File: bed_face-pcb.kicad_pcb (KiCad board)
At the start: 2 copper layers, 98 parts, among them SW1 SW_Push, U1 ProMicro

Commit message: keys placed * may change to my personal layout
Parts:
- moved D37 359.0 mm to (53.2, 132.6), turned to 270 degrees
- moved D25 352.9 mm to (53.2, 113.5), turned to 270 degrees
- moved D38 351.2 mm to (72.2, 132.6), turned to 270 degrees
- moved D39 320.8 mm to (91.3, 132.6), turned to 270 degrees
- moved SW1 298.3 mm to (81.0, 57.1)
- moved D16 294.2 mm to (110.3, 94.5), turned to 270 degrees
- moved D17 287.0 mm to (129.4, 94.5), turned to 270 degrees
- moved D27 280.5 mm to (91.3, 113.5), turned to 270 degrees
- moved D18 269.1 mm to (148.4, 94.5), turned to 270 degrees
- moved D40 265.7 mm to (110.3, 132.6), turned to 270 degrees
- moved D5 261.0 mm to (129.4, 75.4), turned to 270 degrees
- moved D26 256.6 mm to (72.2, 113.6), turned to 270 degrees
- moved D30 249.2 mm to (148.4, 113.5), turned to 270 degrees
- moved D32 239.3 mm to (186.5, 113.5), turned to 270 degrees
- moved D31 233.2 mm to (167.5, 113.5), turned to 270 degrees
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- renumbered D37 to D10, D41 to D11, D45 to D12, D2 to D13, D6 to D14, D10 to D15, D14 to D16, D18 to D17, D22 to D18, D26 to D19, D5 to D2, D30 to D20, D34 to D21, D38 to D22, D42 to D23, D46 to D24, D3 to D25, D7 to D26, D11 to D27, D15 to D28, D19 to D29, D9 to D3, D23 to D30, D27 to D31, D31 to D32, D35 to D33, D39 to D34, D43 to D35, D47 to D36, D4 to D37, D8 to D38, D12 to D39, D13 to D4, D16 to D40, D20 to D41, D24 to D42, D28 to D43, D32 to D44, D36 to D45, D40 to D46, D44 to D47, D17 to D5, D21 to D6, D25 to D7, D29 to D8, D33 to D9, MX37 to MX10, MX41 to MX11, MX45 to MX12, MX2 to MX13, MX6 to MX14, MX10 to MX15, MX14 to MX16, MX18 to MX17, MX22 to MX18, MX26 to MX19, MX5 to MX2, MX30 to MX20, MX34 to MX21, MX38 to MX22, MX42 to MX23, MX46 to MX24, MX3 to MX25, MX7 to MX26, MX11 to MX27, MX15 to MX28, MX19 to MX29, MX9 to MX3, MX23 to MX30, MX27 to MX31, MX31 to MX32, MX35 to MX33, MX39 to MX34, MX43 to MX35, MX47 to MX36, MX4 to MX37, MX8 to MX38, MX12 to MX39, MX13 to MX4, MX16 to MX40, MX20 to MX41, MX24 to MX42, MX28 to MX43, MX32 to MX44, MX36 to MX45, MX40 to MX46, MX44 to MX47, MX17 to MX5, MX21 to MX6, MX25 to MX7, MX29 to MX8, MX33 to MX9

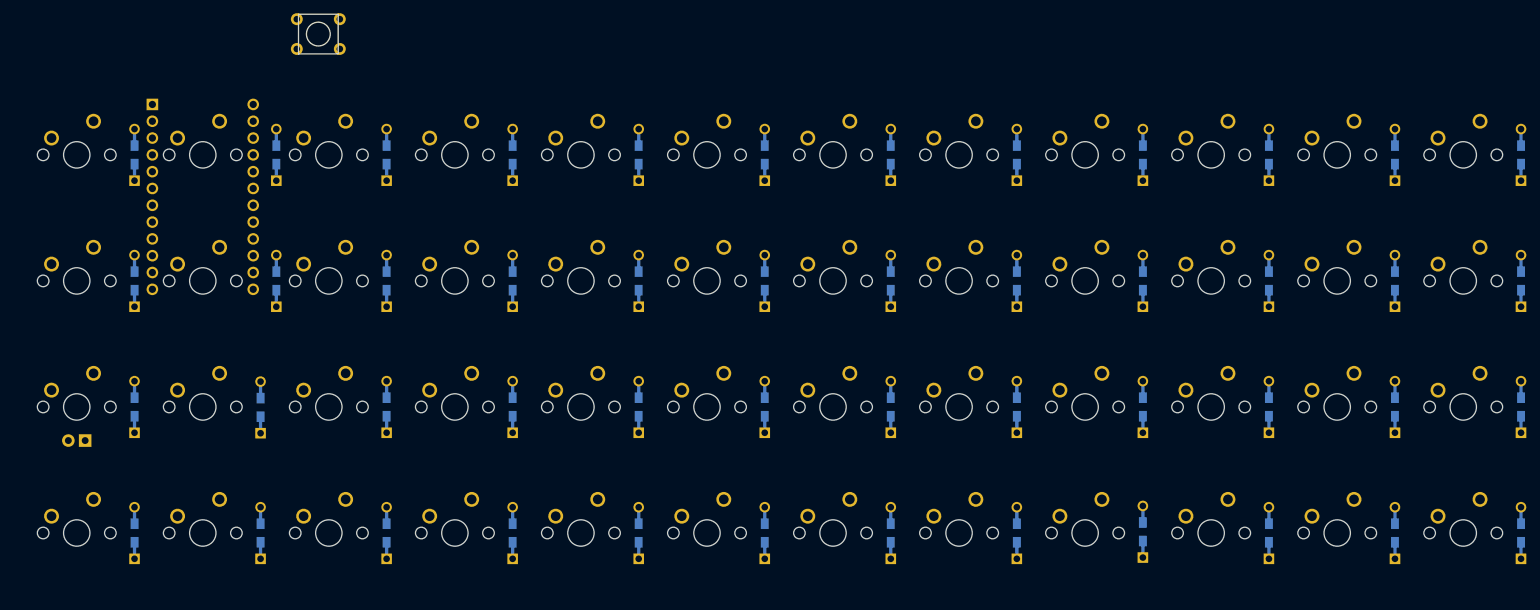
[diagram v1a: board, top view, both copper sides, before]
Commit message: styled switch footprints, initial pcb placement
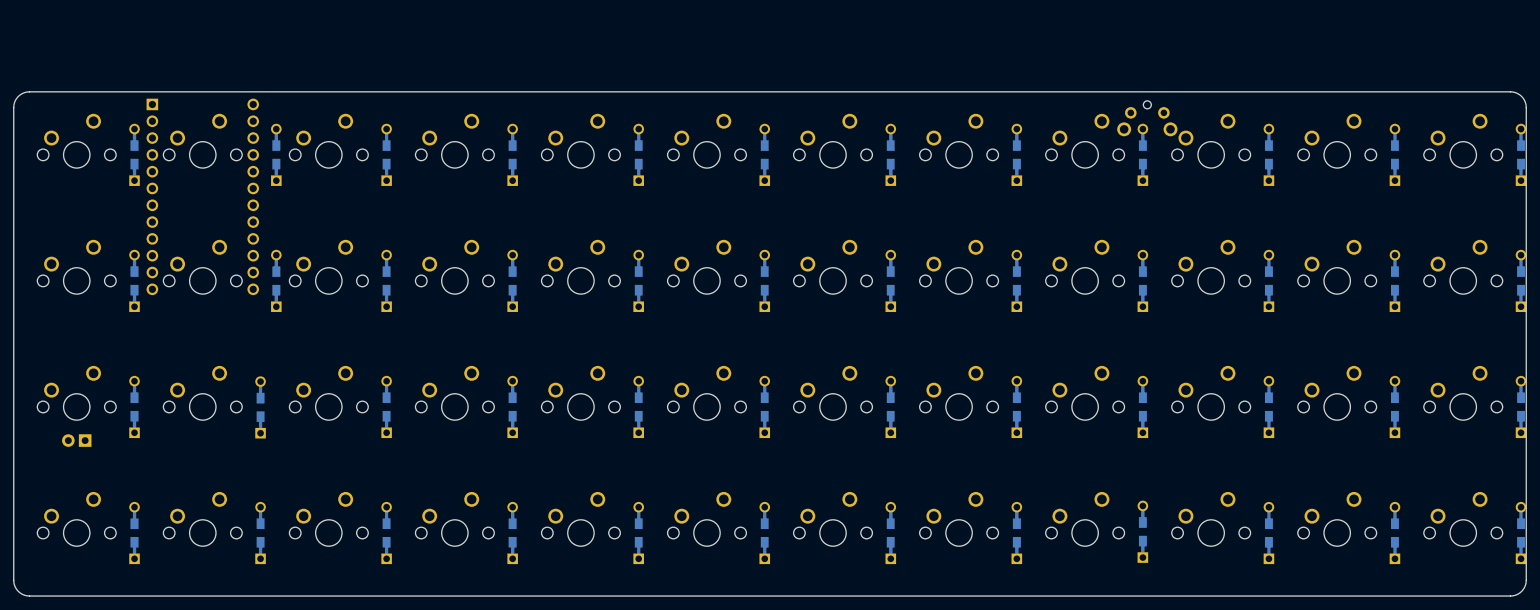
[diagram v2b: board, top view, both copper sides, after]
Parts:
- MX1, MX10, MX11, MX12, MX13, MX14, MX15, MX16, MX17, MX18, MX19, MX2, MX20, MX21, MX22, MX23, MX24, MX26, MX27, MX28, MX29, MX3, MX30, MX31, MX32, MX33, MX34, MX35, MX36, MX37, MX38, MX39, MX4, MX40, MX41, MX42, MX43, MX44, MX45, MX46, MX47, MX48, MX5, MX6, MX7, MX8, MX9: footprint MX_Only:MXOnly-1U-NoLED -> MX_Only:MXOnly-1U-NoLED-EDIT
- MX25: footprint MX_Only:MXOnly-1U -> MX_Only:MXOnly-1U-EDIT
- SW1: footprint random-keyboard-parts:PushButton_6x6mm_TH_Pretty -> Keebio-Parts:SW_Tactile_SPST_Angled_MJTP1117; moved to B.Cu
- moved SW1 128.3 mm to (208.8, 69.1), turned to 180 degrees
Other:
- board outline added: 228.6 x 76.2 mm

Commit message: added +5V, GND to Power net w/ 15 mil track width
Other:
- net class Power added: clearance 0.2, trace_width 0.381, via_dia 0.8, via_drill 0.4
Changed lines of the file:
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@@
     (uvia_dia 0.3)
     (uvia_drill 0.1)
-    (add_net +5V)
     (add_net COL0)
     (add_net COL1)
@@
     (add_net COL8)
     (add_net COL9)
-    (add_net GND)
     (add_net LEDPIN)
     (add_net "Net-(D1-Pad2)")
@@
     (add_net ROW3)
   )
+  (net_class Power ""
+    (clearance 0.2)
+    (trace_width 0.381)
+    (via_dia 0.8)
+    (via_drill 0.4)
+    (uvia_dia 0.3)
+    (uvia_drill 0.1)
+    (add_net +5V)
+    (add_net GND)
+  )
   (module MX_Only:MXOnly-1U-NoLED-EDIT (layer F.Cu)

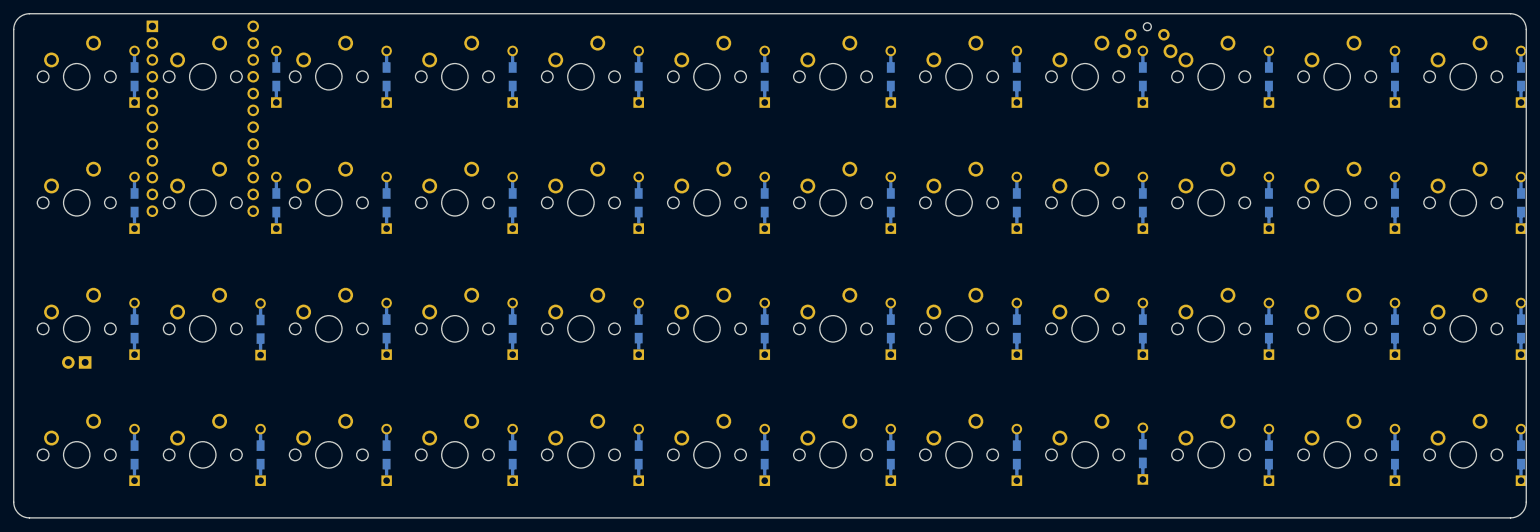
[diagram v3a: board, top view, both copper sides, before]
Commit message: matrix routed, GND fill placed * still needs resistor for LED? * need to add silkscreen/graphic
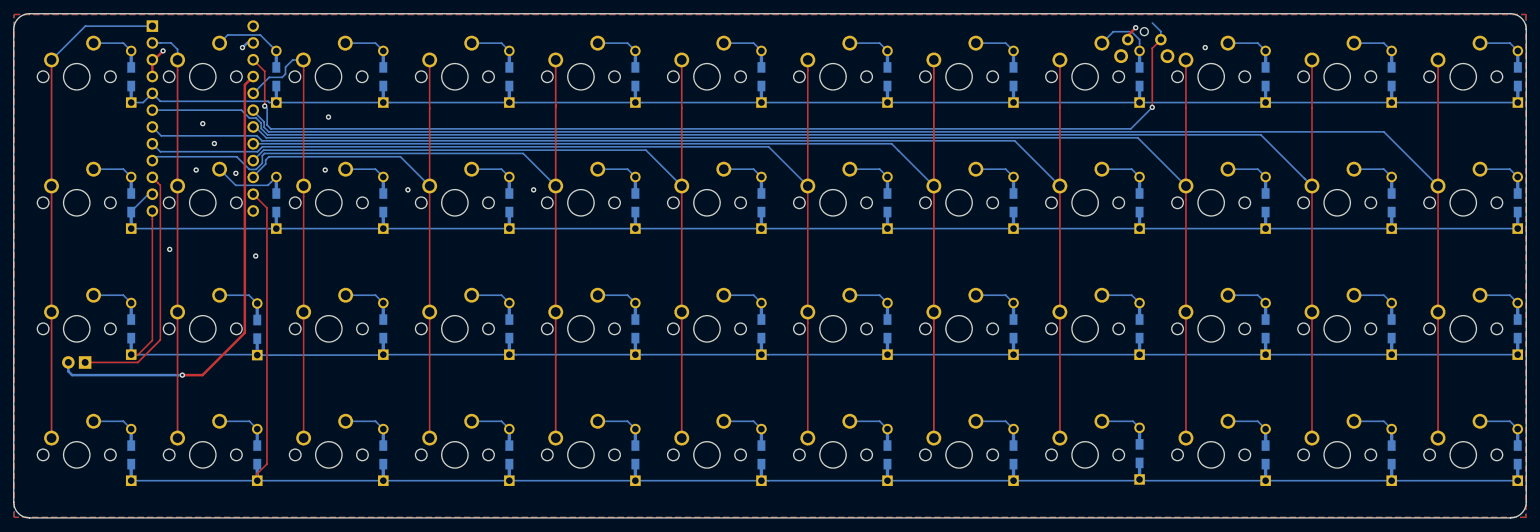
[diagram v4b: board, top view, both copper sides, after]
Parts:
- moved SW1 0.87 mm to (208.3, 69.8)
- moved D1 0.50 mm to (52.7, 75.4)
- moved D10 0.50 mm to (224.1, 75.4)
- moved D11 0.50 mm to (243.2, 75.4)
- moved D13 0.50 mm to (52.7, 94.5)
- moved D15 0.50 mm to (90.8, 94.5)
- moved D16 0.50 mm to (109.8, 94.5)
- moved D17 0.50 mm to (128.9, 94.5)
- moved D18 0.50 mm to (147.9, 94.5)
- moved D19 0.50 mm to (167.0, 94.5)
- moved D20 0.50 mm to (186.0, 94.5)
- moved D21 0.50 mm to (205.1, 94.5)
- moved D22 0.50 mm to (224.1, 94.5)
- moved D23 0.50 mm to (243.2, 94.5)
- moved D24 0.50 mm to (262.2, 94.5)
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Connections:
- net Net-(SW1-Pad1) renamed RESET
- U1 pad 1: Net-(U1-Pad1) -> COL0
- U1 pad 10: Net-(U1-Pad10) -> LEDPIN
- U1 pad 11: Net-(U1-Pad11) -> ROW1
- U1 pad 12: Net-(U1-Pad12) -> ROW2
- U1 pad 14: Net-(U1-Pad14) -> ROW3
- U1 pad 15: Net-(U1-Pad15) -> COL3
- U1 pad 16: Net-(U1-Pad16) -> COL5
- U1 pad 17: Net-(U1-Pad17) -> COL7
- U1 pad 18: Net-(U1-Pad18) -> COL9
- U1 pad 19: Net-(U1-Pad19) -> COL11
- U1 pad 2: Net-(U1-Pad2) -> COL1
- U1 pad 20: Net-(U1-Pad20) -> COL2
- U1 pad 5: Net-(U1-Pad5) -> ROW0
- U1 pad 6: Net-(U1-Pad6) -> COL10
- U1 pad 7: Net-(U1-Pad7) -> COL8
- U1 pad 8: Net-(U1-Pad8) -> COL6
- U1 pad 9: Net-(U1-Pad9) -> COL4
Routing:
- net ROW3: track 0.00 -> 254.5 mm
- net COL11: track 0.00 -> 241.9 mm
- net COL10: track 0.00 -> 238.0 mm
- net ROW2: track 0.00 -> 233.3 mm
- net ROW1: track 0.00 -> 215.0 mm
- net ROW0: track 0.00 -> 210.8 mm
- net COL9: track 0.00 -> 201.8 mm
- net COL8: track 0.00 -> 198.0 mm
- net COL7: track 0.00 -> 162.7 mm
- net RESET: track 0.00 -> 159.9 mm, vias 0 -> 2
- net COL6: track 0.00 -> 159.5 mm
- net COL5: track 0.00 -> 124.8 mm
- net COL4: track 0.00 -> 123.2 mm
- net COL3: track 0.00 -> 87.4 mm
- net COL0: track 0.00 -> 74.5 mm
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- added copper zone on B.Cu, net GND
- added copper zone on F.Cu, net GND

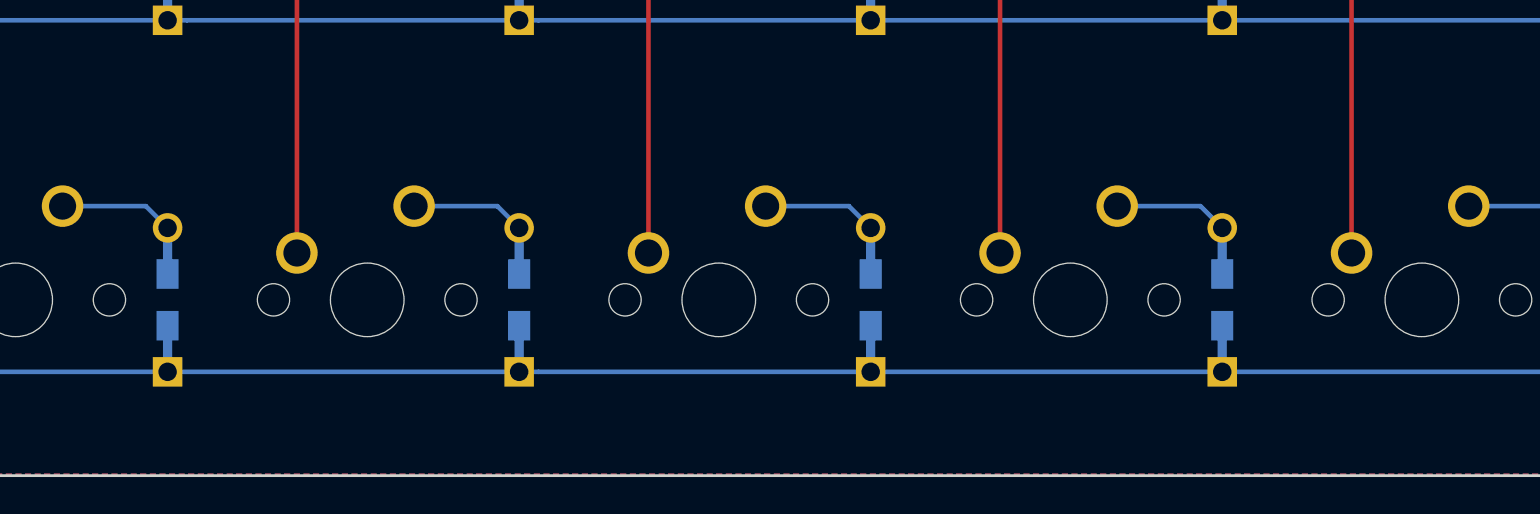
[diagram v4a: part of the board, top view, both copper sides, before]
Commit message: added split vs. 2u space
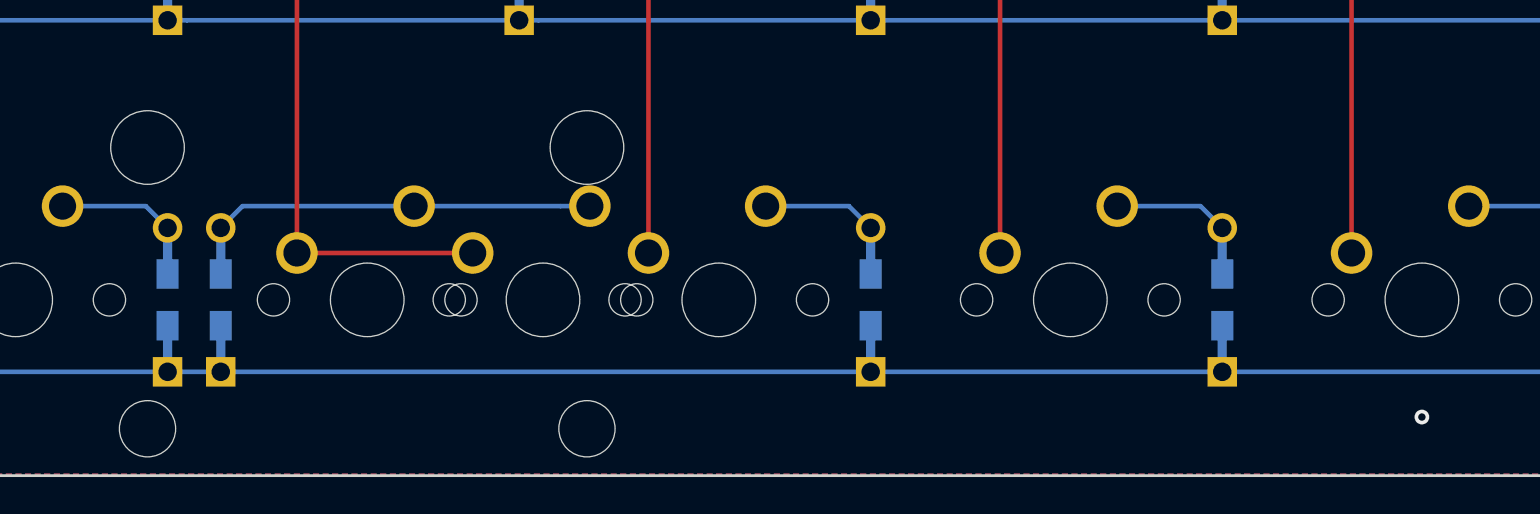
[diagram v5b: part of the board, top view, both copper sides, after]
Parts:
- MX42: footprint MX_Only:MXOnly-1U-NoLED-EDIT -> MX_Only:MXOnly-2U-ReversedStabilizers-NoLED-ComboSpace-EDIT
- moved D42 16.2 mm to (131.8, 132.6)
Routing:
- net Net-(D42-Pad2): track 6.18 -> 20.5 mm
- net COL5: track 124.8 -> 134.3 mm
- net GND: vias 14 -> 15

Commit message: began placing encoders, squaring matrix * squaring matrix gains MCU pins * RE footpints need silkscreen changes
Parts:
- added RE1: Rotary_Encoder_Switch, reversible-kicad-footprints:MX-1U-EC11_Switch, F.Cu at (44.5, 75.4)
- added RE2: Rotary_Encoder_Switch, reversible-kicad-footprints:MX-1U-EC11_Switch, F.Cu at (44.5, 94.5)
- added RE3: Rotary_Encoder_Switch, reversible-kicad-footprints:MX-1U-EC11_Switch, F.Cu at (44.5, 113.5)
- added RE4: Rotary_Encoder_Switch, reversible-kicad-footprints:MX-1U-EC11_Switch, F.Cu at (44.5, 132.6)
- added RE5: Rotary_Encoder_Switch, reversible-kicad-footprints:MX-1U-EC11_Switch, F.Cu at (254.0, 75.4)
- added RE6: Rotary_Encoder_Switch, reversible-kicad-footprints:MX-1U-EC11_Switch, F.Cu at (254.0, 94.5)
- added RE7: Rotary_Encoder_Switch, reversible-kicad-footprints:MX-1U-EC11_Switch, F.Cu at (254.0, 113.5)
- added RE8: Rotary_Encoder_Switch, reversible-kicad-footprints:MX-1U-EC11_Switch, F.Cu at (254.0, 132.6)
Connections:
- net Net-(D1-Pad2) renamed D1
- net Net-(D13-Pad2) renamed D13
- net Net-(D25-Pad2) renamed D25
- net Net-(D37-Pad2) renamed D37
- net Net-(U1-Pad24) renamed BATT+
- D11 pad 1: ROW0 -> Net-(D11-Pad1)
- D12 pad 1: ROW0 -> Net-(D12-Pad1)
- D23 pad 1: ROW1 -> Net-(D23-Pad1)
- D24 pad 1: ROW1 -> Net-(D24-Pad1)
- D35 pad 1: ROW2 -> Net-(D35-Pad1)
- D36 pad 1: ROW2 -> Net-(D36-Pad1)
- D47 pad 1: ROW3 -> Net-(D47-Pad1)
- D48 pad 1: ROW3 -> Net-(D48-Pad1)
- MX11 pad 1: COL10 -> Net-(MX11-Pad1)
- MX12 pad 1: COL11 -> COL2
- MX23 pad 1: COL10 -> Net-(MX23-Pad1)
- MX24 pad 1: COL11 -> Net-(MX24-Pad1)
- MX35 pad 1: COL10 -> Net-(MX35-Pad1)
- MX36 pad 1: COL11 -> Net-(MX36-Pad1)
- MX47 pad 1: COL10 -> Net-(MX47-Pad1)
- MX48 pad 1: COL11 -> Net-(MX48-Pad1)
- U1 pad 19: COL11 -> EB
- U1 pad 6: COL10 -> EA
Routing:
- net COL11: track 241.9 -> 0.00 mm
- net COL10: track 238.0 -> 0.00 mm
- net EB: track 0.00 -> 173.1 mm
- net EA: track 0.00 -> 169.9 mm
- net ROW0: track 210.8 -> 172.6 mm
- net ROW1: track 215.0 -> 176.9 mm
- net ROW3: track 254.5 -> 216.4 mm
- net ROW2: track 233.3 -> 195.2 mm
- net +5V: track 70.2 -> 51.9 mm
- net COL0: track 74.5 -> 57.2 mm
- net RESET: track 159.9 -> 156.9 mm

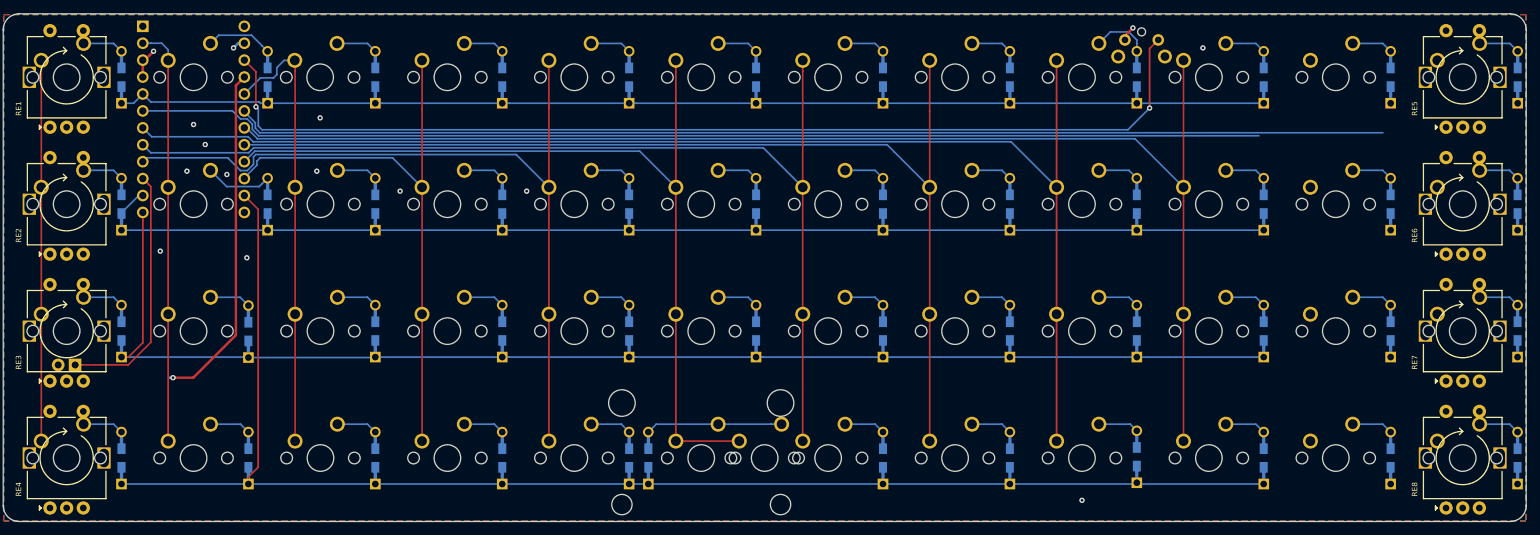
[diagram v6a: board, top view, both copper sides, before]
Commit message: squared up matrix, placed + tracked encoders * encoder support for first and last columns * needs battery connector * encoder silks need changing
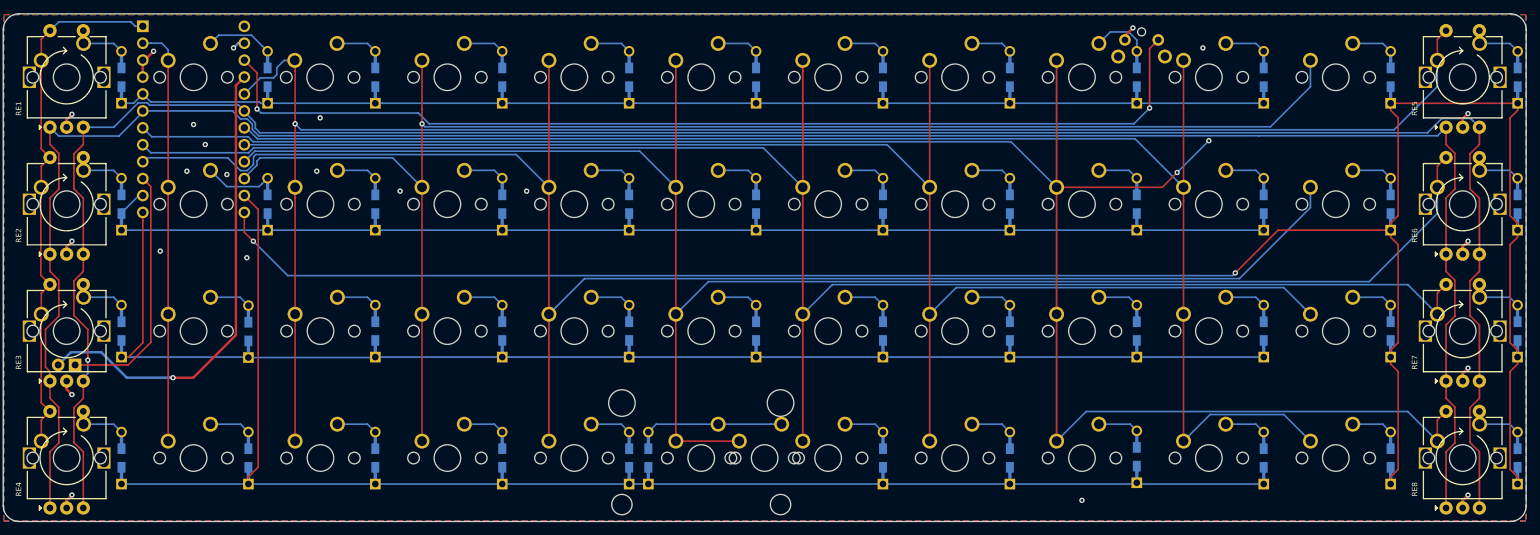
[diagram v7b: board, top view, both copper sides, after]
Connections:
- D11 pad 1: Net-(D11-Pad1) -> ROW4
- D12 pad 1: Net-(D12-Pad1) -> ROW4
- D12 pad 2: Net-(D12-Pad2) -> D12
- D23 pad 1: Net-(D23-Pad1) -> ROW4
- D24 pad 1: Net-(D24-Pad1) -> ROW4
- D24 pad 2: Net-(D24-Pad2) -> D24
- D35 pad 1: Net-(D35-Pad1) -> ROW4
- D36 pad 1: Net-(D36-Pad1) -> ROW4
- D36 pad 2: Net-(D36-Pad2) -> D36
- D47 pad 1: Net-(D47-Pad1) -> ROW4
- D48 pad 1: Net-(D48-Pad1) -> ROW4
- D48 pad 2: Net-(D48-Pad2) -> D48
- MX11 pad 1: Net-(MX11-Pad1) -> COL3
- MX12 pad 2: Net-(D12-Pad2) -> D12
- MX23 pad 1: Net-(MX23-Pad1) -> COL4
- MX24 pad 1: Net-(MX24-Pad1) -> COL5
- MX24 pad 2: Net-(D24-Pad2) -> D24
- MX35 pad 1: Net-(MX35-Pad1) -> COL7
- MX36 pad 1: Net-(MX36-Pad1) -> COL6
- MX36 pad 2: Net-(D36-Pad2) -> D36
- MX47 pad 1: Net-(MX47-Pad1) -> COL9
- MX48 pad 1: Net-(MX48-Pad1) -> COL8
- MX48 pad 2: Net-(D48-Pad2) -> D48
- RE2 pad S1: COL1 -> D13
- RE2 pad S2: D13 -> COL0
- RE3 pad S1: COL2 -> D25
- RE3 pad S2: D25 -> COL0
- RE4 pad S1: COL3 -> D37
- RE4 pad S2: D37 -> COL0
- RE5 pad S1: Net-(RE5-PadS1) -> D12
- RE5 pad S2: Net-(RE5-PadS2) -> COL2
- RE6 pad S1: Net-(RE6-PadS1) -> D24
- RE6 pad S2: Net-(RE6-PadS2) -> COL5
- RE7 pad S1: Net-(RE7-PadS1) -> D36
- RE7 pad S2: Net-(RE7-PadS2) -> COL6
- RE8 pad S1: Net-(RE8-PadS1) -> D48
- RE8 pad S2: Net-(RE8-PadS2) -> COL8
- U1 pad 13: Net-(U1-Pad13) -> ROW4
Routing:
- net ROW4: track 0.00 -> 319.5 mm, vias 0 -> 2
- net COL2: track 67.4 -> 250.9 mm, vias 0 -> 1
- net EA: track 169.9 -> 336.1 mm
- net EB: track 173.1 -> 337.1 mm, vias 0 -> 1
- net COL3: track 87.4 -> 227.4 mm, vias 0 -> 1
- net COL5: track 134.3 -> 263.8 mm
- net COL4: track 123.2 -> 247.2 mm
- net COL6: track 159.5 -> 263.4 mm
- net COL8: track 198.0 -> 289.6 mm, vias 0 -> 2
- net COL7: track 162.7 -> 223.1 mm
- net COL0: track 57.2 -> 80.2 mm
- net COL9: track 201.8 -> 224.2 mm
- net +5V: track 51.9 -> 70.9 mm
- net GND: track 8.92 -> 27.3 mm, vias 15 -> 23
- net D12: track 0.00 -> 8.14 mm
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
